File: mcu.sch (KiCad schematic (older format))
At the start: 8 parts

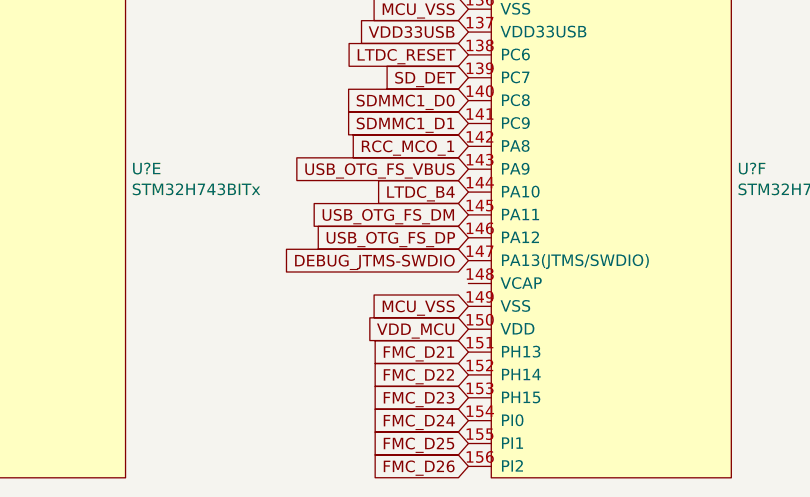
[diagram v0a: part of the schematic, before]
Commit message: First proposed pin layout of SODIMM connector
Will need to add GPIO / ADC pins as needed, but let's wait to see if we don't
need to use more pins.

Double-checked and fixed CODEC and MCU's power supply.
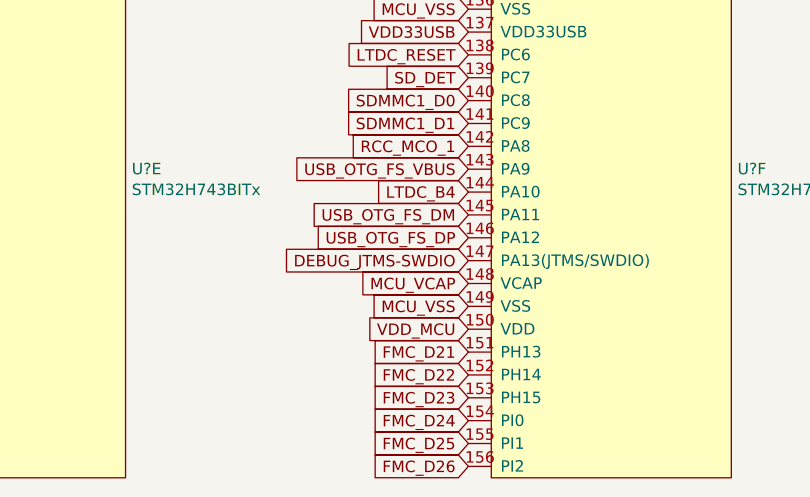
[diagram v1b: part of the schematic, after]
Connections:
- net MCU_VCAP: now also U?.148 (VCAP)
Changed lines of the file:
@@
 $Descr A4 11693 8268
 encoding utf-8
-Sheet 2 12
+Sheet 2 13
 Title ""
 Date ""
@@
 Text GLabel 4150 4250 0    50   Input ~ 0
 LTDC_RESET
+Text GLabel 4150 5250 0    50   Input ~ 0
+MCU_VCAP
 $EndSCHEMATC
